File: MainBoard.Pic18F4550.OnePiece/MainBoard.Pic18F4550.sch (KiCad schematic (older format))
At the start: 83 parts, among them CON1 USB_CON, J1 VIKING_CON_9P, J10 IO_CON_8P, J11 PORTB_CON_6P, J12 PORTCD_CON_5P, J13 PORTA_CON_7P, J2 GPIB_CON_9P, J3 VIKING_CON_9P, J4 GPIB_CON_9P, J5 POWER_CON_01X06, J6 VIKING_CON_01X09, J7 VIKING_CON_01X09, J8 RESET_CON_01X02, J9 IO_CON_8P, U1 PCA6416A, U2 PIC18F4550-I/P, U3 MC33996EKR2, U4 MC33996EKR2, U5 PCA6416A, Y1 20MHZ

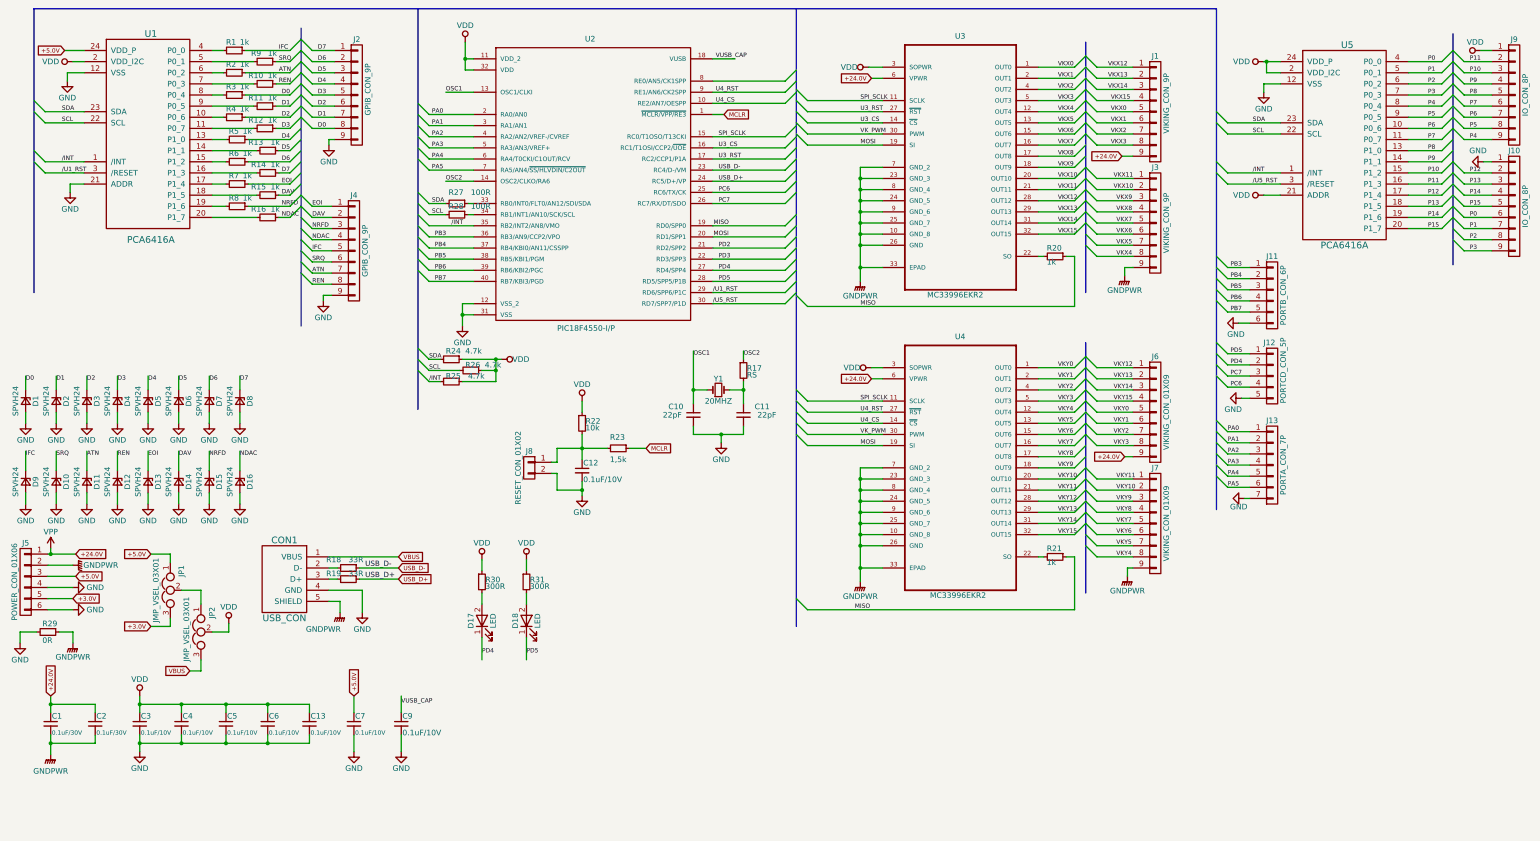
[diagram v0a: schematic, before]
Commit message: Revision de PCBs + MergedPcbs
  - Se revisan PCBs
      - VikingPortExpander
      - GpibPortExpander
      - MainBoards en tres versiones
  - Se genera archivos Gerber que combina estos PCBs en un documento
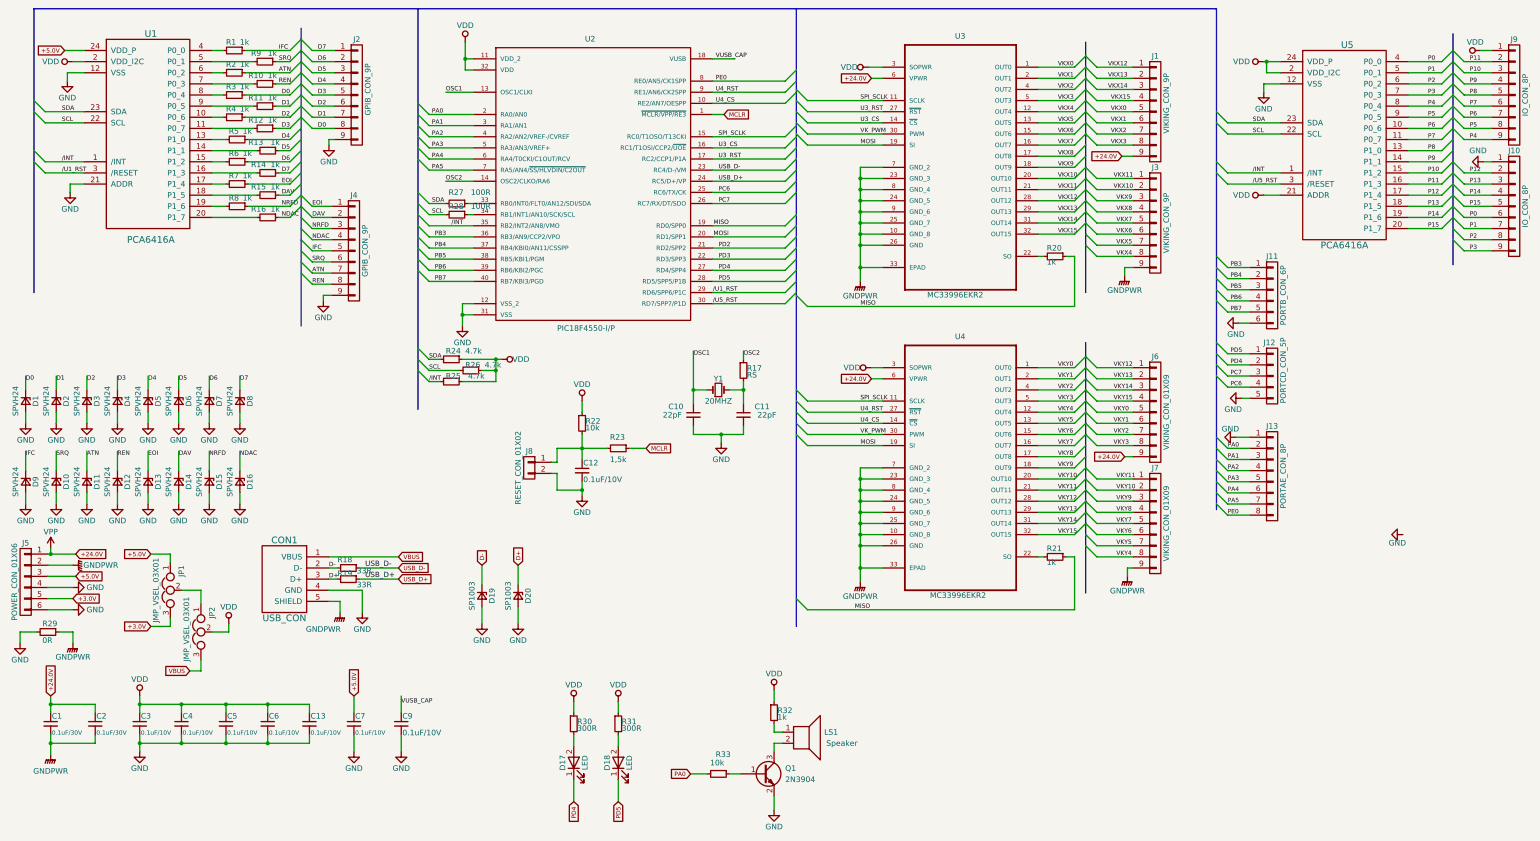
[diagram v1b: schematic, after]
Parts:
- removed J13: PORTA_CON_7P, Pin_Headers:Pin_Header_Straight_1x07_Pitch2.54mm, symbol CONN_01X07
- added D19, D20: SP1003, CenditFootprints:SP1003-01ETG, symbol D_Zener_Small
- added J13: PORTAE_CON_8P, Pin_Headers:Pin_Header_Straight_1x08_Pitch2.54mm, symbol CONN_01X08
- added LS1: Speaker, Buzzers_Beepers:MagneticBuzzer_Kingstate_KCG0601, symbol Speaker
- added Q1: 2N3904, TO_SOT_Packages_SMD:SOT-23, symbol Q_NPN_BEC
- added R32: 1k, Resistors_SMD:R_0805_HandSoldering, symbol R_Small
- added R33: 10k, Resistors_SMD:R_0805_HandSoldering, symbol R_Small
- Y1: footprint Crystals:Crystal_HC52-6mm_Vertical -> Crystals:Crystal_SMD_HC49-SD
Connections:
- net labels added: D+, D-, PE0
- wire segments 396 -> 409
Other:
- moved on the sheet: D17, D18, R30, R31
